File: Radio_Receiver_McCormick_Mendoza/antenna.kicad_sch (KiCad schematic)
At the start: 18 parts, among them J5 Conn_Coaxial, J5 FIL_IN, J8 FIL_OUT, SW1 SW_Slide_DPDT, SW2 SW_Slide_DPDT, T1 Transformer_1P_SS

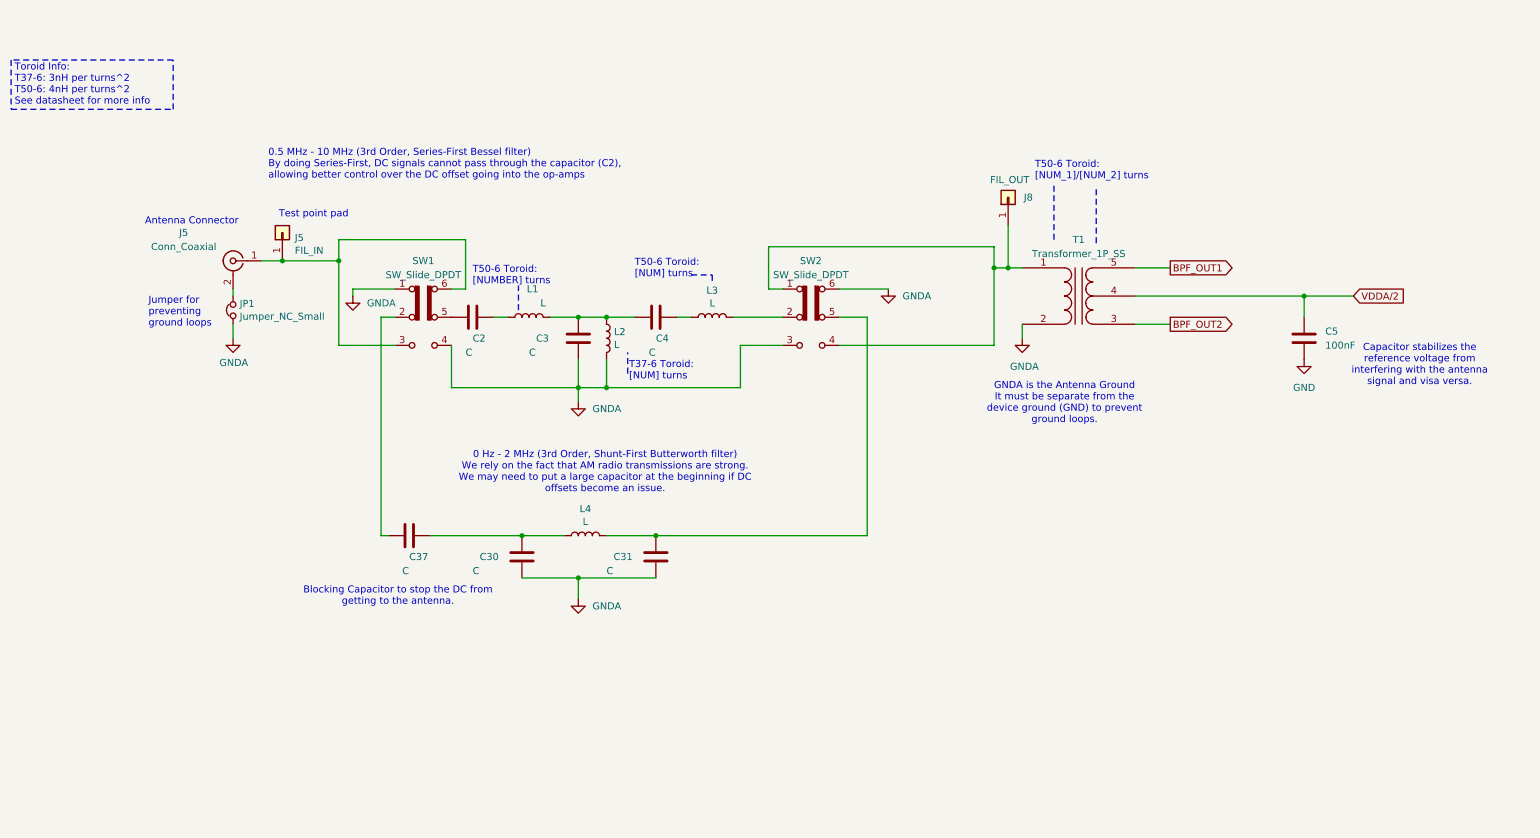
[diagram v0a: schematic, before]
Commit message: Isolated filter switching MUX from digital control
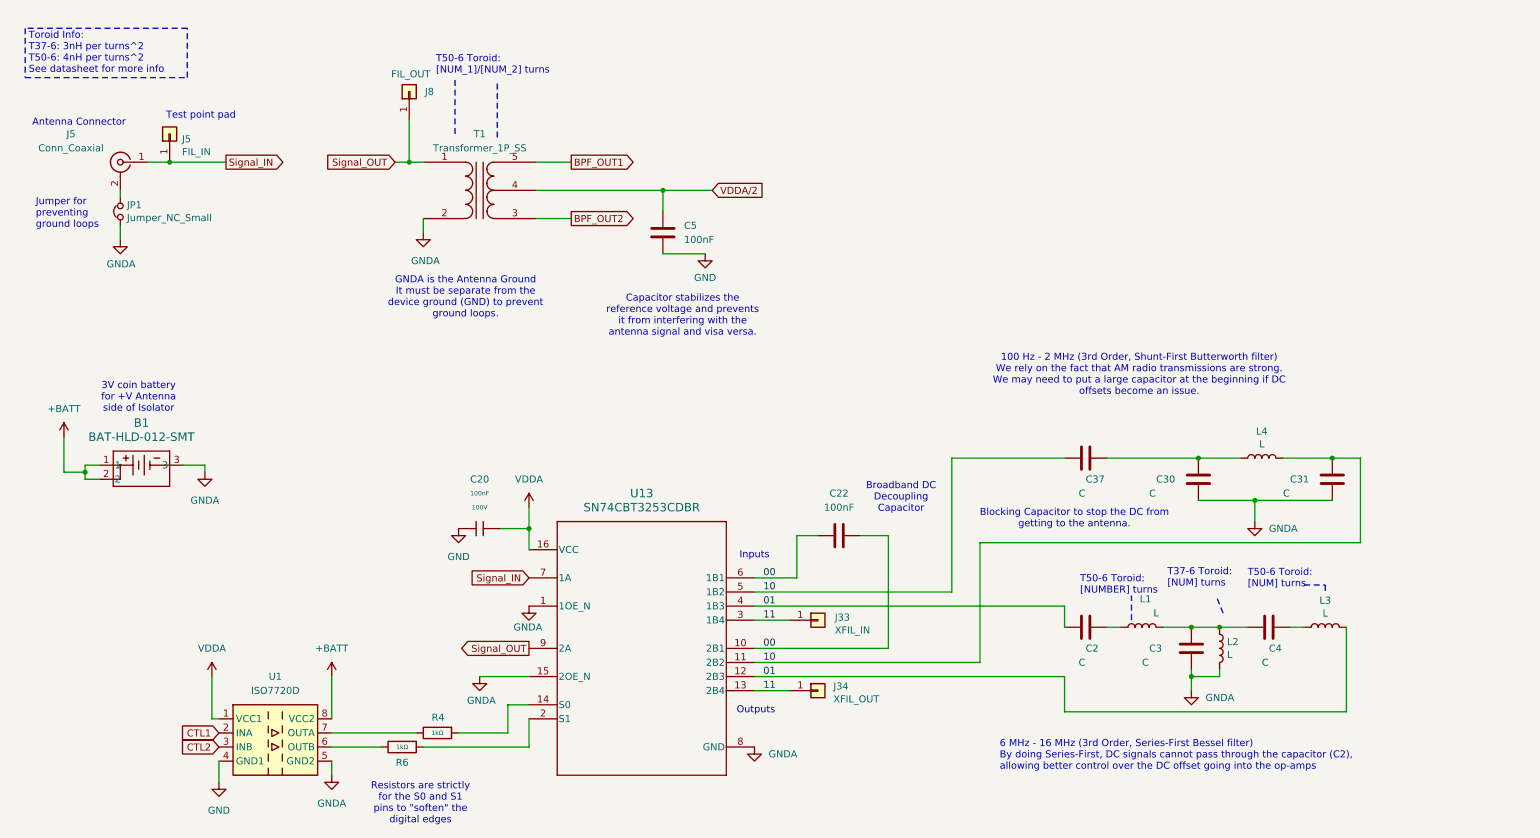
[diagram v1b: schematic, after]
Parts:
- removed SW1, SW2: SW_Slide_DPDT, symbol Switch:SW_Slide_DPDT
- added B1: BAT-HLD-012-SMT, BATTTERY_HOLDER_12mm_SMT:BAT-HLD-012-SMT_TEC, symbol BATTERY_HOLDER_12mm_SMT:BAT-HLD-012-SMT
- added C20: 100nF, PCM_JLCPCB:C_0805, symbol PCM_JLCPCB-Capacitors:0805,100nF
- added C22: 100nF, PCM_JLCPCB:C_1206, symbol Device:C
- added J33: XFIL_IN, Connector_PinHeader_2.54mm:PinHeader_1x01_P2.54mm_Vertical, symbol SDRReciever-rescue:Conn_01x01-Connector_Generic-SDRReciever-rescue
- added J34: XFIL_OUT, Connector_PinHeader_2.54mm:PinHeader_1x01_P2.54mm_Vertical, symbol SDRReciever-rescue:Conn_01x01-Connector_Generic-SDRReciever-rescue
- added R4, R6: 1kΩ, PCM_JLCPCB:R_0402, symbol PCM_JLCPCB-Resistors:0402,1kΩ
- added U1: ISO7720D, Package_SO:SOIC-8_3.9x4.9mm_P1.27mm, symbol Isolator:ISO7720D
- added U13: SN74CBT3253CDBR, SN74CBT3253CDBR_1-4_MUX:DB0016A_N, symbol SN74CBT3253CDBR:SN74CBT3253CDBR
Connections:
- net GND: now also C20.1, U1.4 (GND1)
- net GNDA: now also B1.3, U1.5 (GND2), U13.1 (1OE_N), U13.15 (2OE_N), U13.8 (GND)
- net Signal_OUT: now reaches J8.1 (Pin_1), T1.1 (AA)
- net Signal_OUT: now also U13.9 (2A)
- net 01: now reaches L3.2
- net 01: now also C2.1, U13.12 (2B3), U13.4 (1B3)
- net 10: now reaches C31.2, L4.2
- net 10: now also C37.1, U13.11 (2B2), U13.5 (1B2)
- net Signal_IN: now reaches J5.1 (In), J5.1 (Pin_1)
- net Signal_IN: now also U13.7 (1A)
- new net: R4.1, U13.14 (S0)
- new net: R4.2, U1.7 (OUTA)
- new net: R6.2, U1.6 (OUTB)
- new net: R6.1, U13.2 (S1)
- new net +BATT: B1.1, B1.2, U1.8 (VCC2)
- new net 00: C22.1, C22.2, U13.10 (2B1), U13.6 (1B1)
- new net 11: J33.1 (Pin_1), J34.1 (Pin_1), U13.13 (2B4), U13.3 (1B4)
- new net CTL1: U1.2 (INA)
- new net CTL2: U1.3 (INB)
- new net VDDA: C20.2, U1.1 (VCC1), U13.16 (VCC)
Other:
- note added: "100 Hz - 2 MHz (3rd Order, Shunt-First Butterworth filter) We rely on the fact that AM radio transmissions are strong. We may need to put a large capacitor at the beginning if DC offsets become an issue."
- note added: "3V coin battery for +V Antenna side of Isolator"
- note added: "6 MHz - 16 MHz (3rd Order, Series-First Bessel filter) By doing Series-First, DC signals cannot pass through the capacitor (C2), allowing better control over the DC offset going into the op-amps"
- note added: "Broadband DC Decoupling Capacitor"
- note added: "Capacitor stabilizes the reference voltage and prevents it from interfering with the antenna signal and visa versa."
- note added: "Inputs"
- note added: "Outputs"
- note added: "Resistors are strictly for the S0 and S1 pins to "soften" the digital edges"
- note removed: "0 Hz - 2 MHz (3rd Order, Shunt-First Butterworth filter) We rely on the fact that AM radio transmissions are strong. We may need to put a large capacitor at the beginning if DC offsets become an issue."
- note removed: "0.5 MHz - 10 MHz (3rd Order, Series-First Bessel filter) By doing Series-First, DC signals cannot pass through the capacitor (C2), allowing better control over the DC offset going into the op-amps"
- note removed: "Capacitor stabilizes the reference voltage from interfering with the antenna signal and visa versa."
- moved on the sheet: C2, C3, C30, C31, C37, C4, C5, J5, J8, JP1, L1, L2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

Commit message: Added digital power regulator
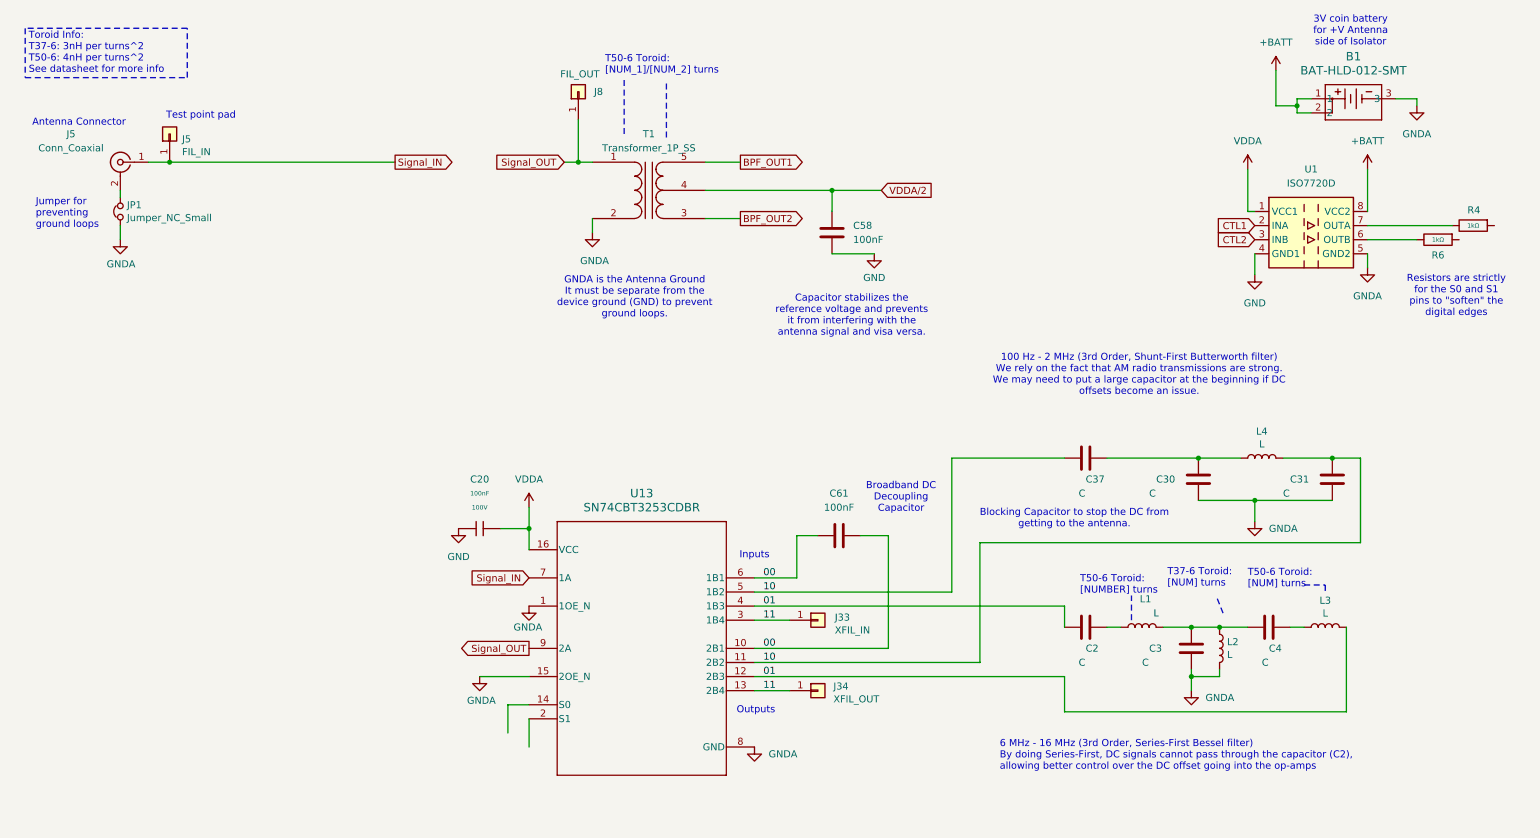
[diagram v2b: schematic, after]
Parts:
- removed C22, C5: 100nF, PCM_JLCPCB:C_1206, symbol Device:C
- added C58, C61: 100nF, PCM_JLCPCB:C_1206, symbol Device:C
- C20: Manufacturer Samsung Electro-Mechanics -> (none)
- R4, R6: Manufacturer UNI-ROYAL(Uniroyal Elec) -> (none)
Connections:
- net 00: now also C61.1, C61.2
- net GND: now also C58.2
- net VDDA/2: now also C58.1
- net at R4.1: no longer U13.14 (S0)
- net at R6.1: no longer U13.2 (S1)
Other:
- moved on the sheet: B1, J8, R4, R6, T1, U1

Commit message: Integrated signal path modules
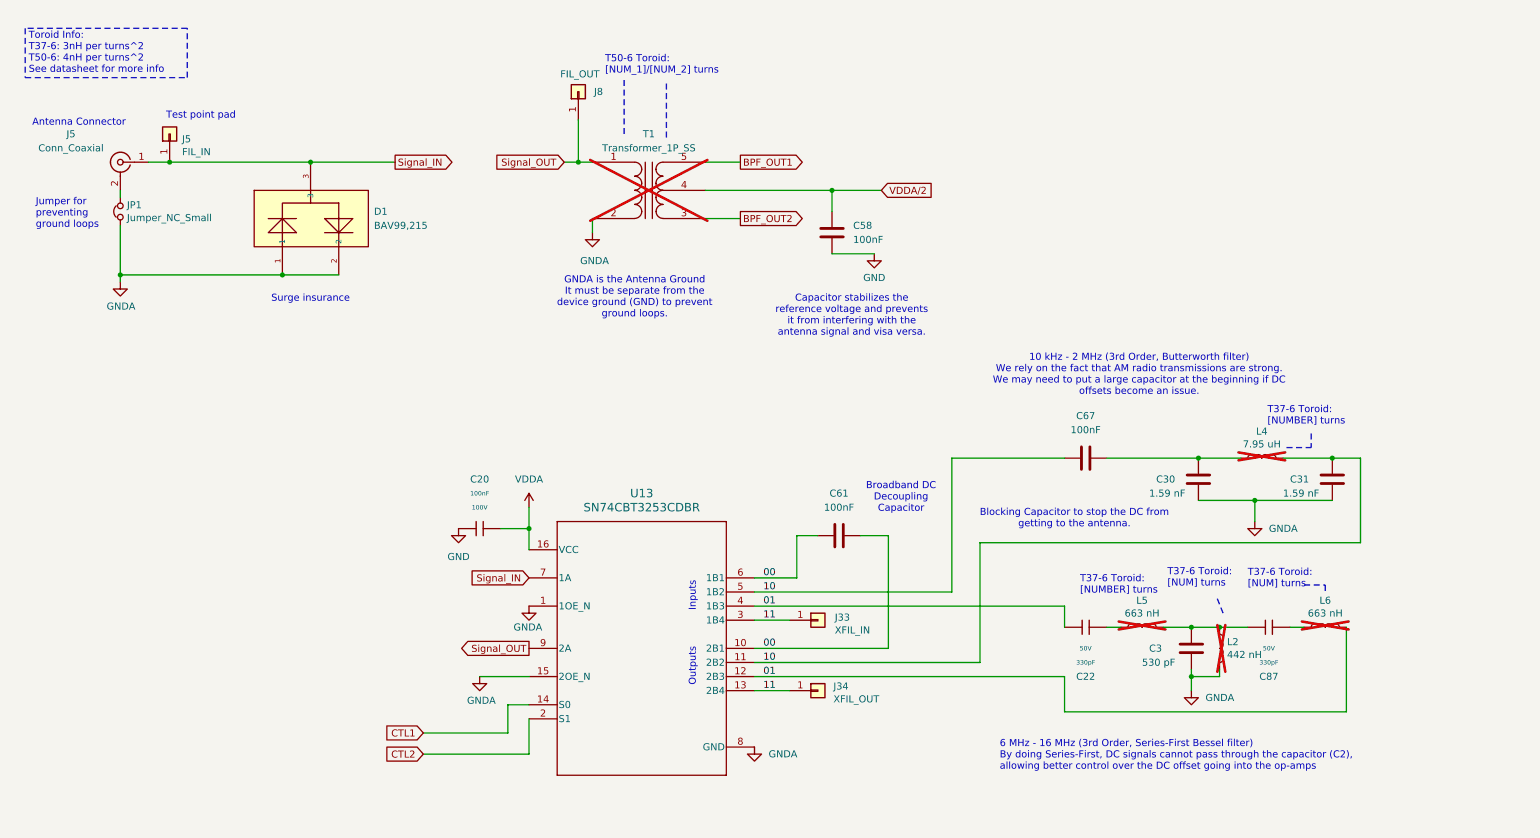
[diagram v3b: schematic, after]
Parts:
- removed B1: BAT-HLD-012-SMT, BATTTERY_HOLDER_12mm_SMT:BAT-HLD-012-SMT_TEC, symbol BATTERY_HOLDER_12mm_SMT:BAT-HLD-012-SMT
- removed C2, C37, C4: C, Capacitor_SMD:C_0805_2012Metric, symbol SDRReciever-rescue:C-Device-SDRReciever-rescue
- removed L1, L3: L, Inductor_THT:L_Toroid_Vertical_L13.0mm_W6.5mm_P5.60mm, symbol SDRReciever-rescue:L-Device-SDRReciever-rescue
- removed R4, R6: 1kΩ, PCM_JLCPCB:R_0402, symbol PCM_JLCPCB-Resistors:0402,1kΩ
- removed U1: ISO7720D, Package_SO:SOIC-8_3.9x4.9mm_P1.27mm, symbol Isolator:ISO7720D
- added C22, C87: 330pF, PCM_JLCPCB:C_0603, symbol PCM_JLCPCB-Capacitors:0603,330pF
- added C67: 100nF, PCM_JLCPCB:C_1206, symbol Device:C
- added D1: BAV99,215, PCM_JLCPCB:SOT-23-3_L3.0-W1.7-P0.95-LS2.9-BR, symbol PCM_JLCPCB-Diode-Packages:Switching, BAV99,215
- added L5, L6: 663 nH, Inductor_THT:L_Toroid_Vertical_L13.0mm_W6.5mm_P5.60mm, symbol SDRReciever-rescue:L-Device-SDRReciever-rescue
- C3: value C -> 530 pF
- C30, C31: value C -> 1.59 nF
- L2: value L -> 442 nH; now not fitted
- L4: value L -> 7.95 uH; now not fitted
- T1: now not fitted
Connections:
- net 01: now also C22.1, L6.2
- net 10: now also C67.1
- net CTL1: now also U13.14 (S0)
- net CTL2: now also U13.2 (S1)
- net GNDA: now also D1.1, D1.2
- net Signal_IN: now also D1.3
- net at C3.2, L2.1: now also C87.1, L5.2
- net at C30.2, L4.1: now also C67.2
- new net: C22.2, L5.1
- new net: C87.2, L6.1
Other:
- note added: "10 kHz - 2 MHz (3rd Order, Butterworth filter) We rely on the fact that AM radio transmissions are strong. We may need to put a large capacitor at the beginning if DC offsets become an issue."
- note added: "Surge insurance"
- note added: "T37-6 Toroid: [NUMBER] turns"
- note removed: "100 Hz - 2 MHz (3rd Order, Shunt-First Butterworth filter) We rely on the fact that AM radio transmissions are strong. We may need to put a large capacitor at the beginning if DC offsets become an issue."
- note removed: "3V coin battery for +V Antenna side of Isolator"
- note removed: "Resistors are strictly for the S0 and S1 pins to "soften" the digital edges"
- note removed: "T50-6 Toroid: [NUMBER] turns"
- note removed: "T50-6 Toroid: [NUM] turns"

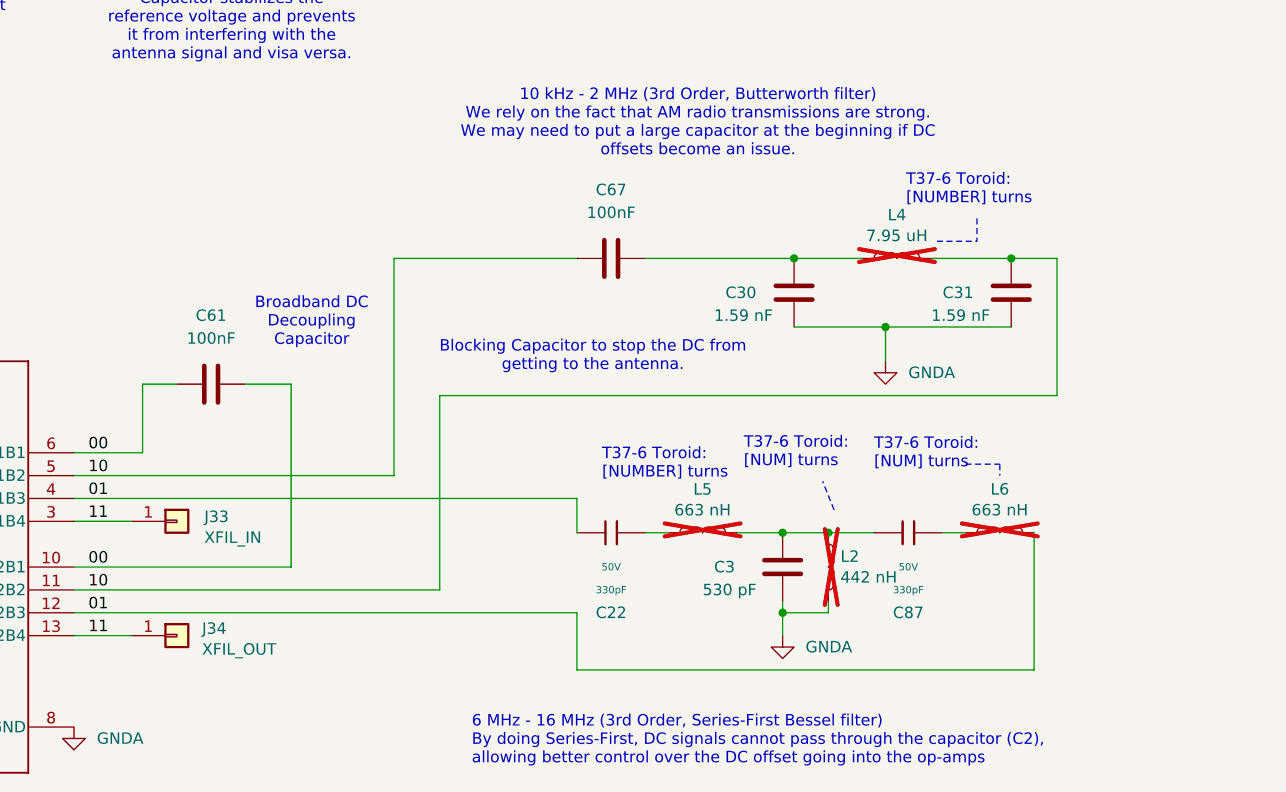
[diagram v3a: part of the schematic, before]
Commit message: Adjusted RF filters for basic component values
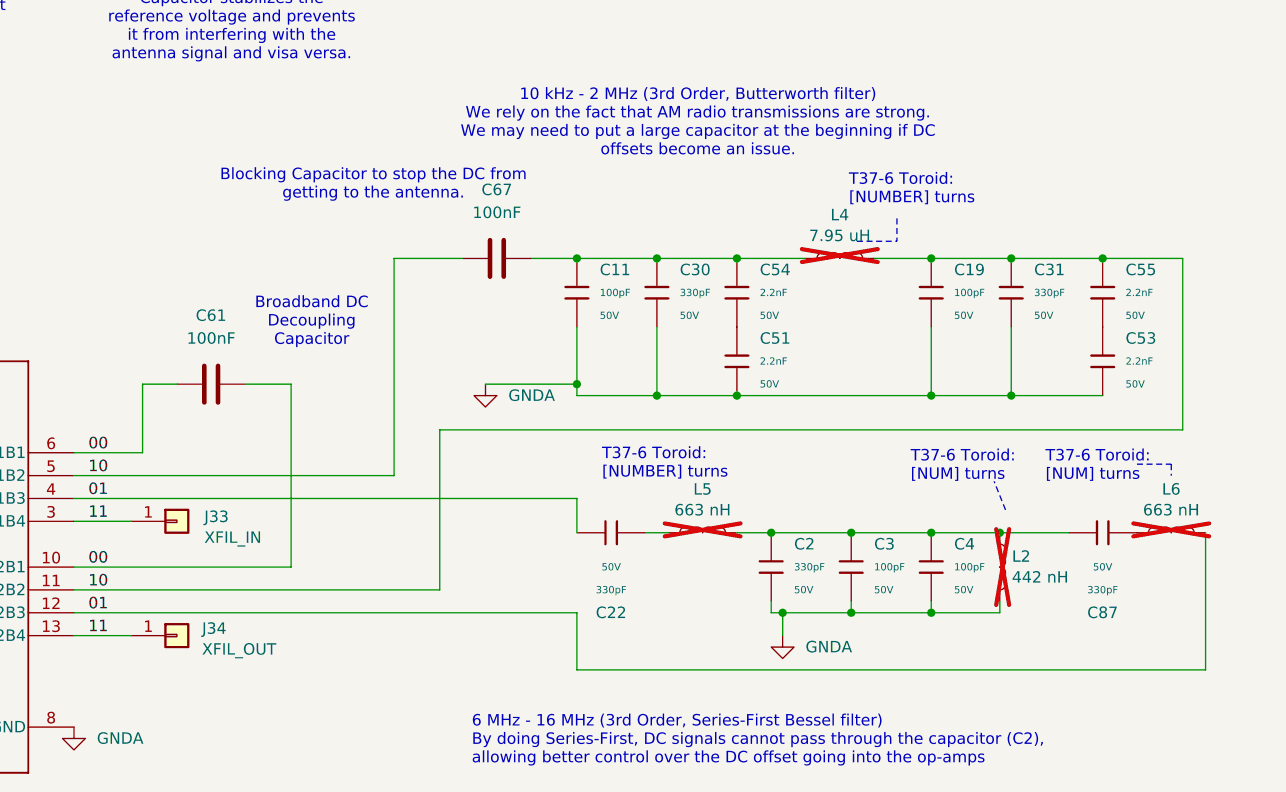
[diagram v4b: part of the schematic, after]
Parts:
- removed C3: 530 pF, Capacitor_SMD:C_0805_2012Metric, symbol SDRReciever-rescue:C-Device-SDRReciever-rescue
- removed C30, C31: 1.59 nF, Capacitor_SMD:C_0805_2012Metric, symbol SDRReciever-rescue:C-Device-SDRReciever-rescue
- added C11, C19, C3, C4: 100pF, PCM_JLCPCB:C_0402, symbol PCM_JLCPCB-Capacitors:0402,100pF
- added C2, C30, C31: 330pF, PCM_JLCPCB:C_0603, symbol PCM_JLCPCB-Capacitors:0603,330pF
- added C51, C53, C54, C55: 2.2nF, PCM_JLCPCB:C_0805, symbol PCM_JLCPCB-Capacitors:0805,2.2nF
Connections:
- net 10: now also C19.1, C31.1, C55.1
- net GNDA: now also C11.2, C19.2, C2.2, C3.2, C30.2, C31.2, C4.2, C51.2, C53.2
- net at C87.1, L2.1, L5.2: now also C2.1, C3.1, C4.1
- net at C67.2, L4.1: now also C11.1, C30.1, C54.1
- new net: C51.1, C54.2
- new net: C53.1, C55.2
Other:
- moved on the sheet: C67, C87, L2, L4, L6
